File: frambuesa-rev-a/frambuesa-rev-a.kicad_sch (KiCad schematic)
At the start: 0 parts

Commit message: agregar chip y conexiones
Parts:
- added C1, C9: 1u, symbol Device:C
- added C10, C11, C2, C3, C4, C5, C6, C7, C8: 100n, symbol Device:C
- added R1, R2: R, symbol Device:R
- added U1: RP2040, Package_DFN_QFN:QFN-56-1EP_7x7mm_P0.4mm_EP3.2x3.2mm, symbol MCU_RaspberryPi:RP2040
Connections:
- new net: R2.2, U1.47 (USB_DP)
- new net: R1.2, U1.46 (USB_DM)
- new net +1V1: C10.1, C11.1, C9.1, U1.23 (DVDD), U1.45 (VREG_VOUT), U1.50 (DVDD)
- new net +3V3: C1.1, C2.1, C3.1, C4.1, C5.1, C6.1, C7.1, C8.1, U1.1 (IOVDD), U1.10 (IOVDD), U1.22 (IOVDD), U1.33 (IOVDD), U1.42 (IOVDD), U1.43 (ADC_AVDD), U1.44 (VREG_VIN), U1.48 (USB_VDD), U1.49 (IOVDD)
- new net GND: C1.2, C10.2, C11.2, C2.2, C3.2, C4.2, C5.2, C6.2, C7.2, C8.2, C9.2, U1.19 (TESTEN), U1.57 (GND)
- new net GPIO00: U1.2 (GPIO0)
- new net GPIO01: U1.3 (GPIO1)
- new net GPIO02: U1.4 (GPIO2)
- new net GPIO03: U1.5 (GPIO3)
- new net GPIO04: U1.6 (GPIO4)
- new net GPIO05: U1.7 (GPIO5)
- new net GPIO06: U1.8 (GPIO6)
- new net GPIO07: U1.9 (GPIO7)
- new net GPIO08: U1.11 (GPIO8)
- new net GPIO09: U1.12 (GPIO9)
- new net GPIO10: U1.13 (GPIO10)
- new net GPIO11: U1.14 (GPIO11)
- new net GPIO12: U1.15 (GPIO12)
- new net GPIO13: U1.16 (GPIO13)
- new net GPIO14: U1.17 (GPIO14)
- new net GPIO15: U1.18 (GPIO15)
- new net GPIO16: U1.27 (GPIO16)
- new net GPIO17: U1.28 (GPIO17)
- new net GPIO18: U1.29 (GPIO18)
- new net GPIO19: U1.30 (GPIO19)
- new net GPIO20: U1.31 (GPIO20)
- new net GPIO21: U1.32 (GPIO21)
- new net GPIO22: U1.34 (GPIO22)
- new net GPIO23: U1.35 (GPIO23)
- new net GPIO24: U1.36 (GPIO24)
- new net GPIO25: U1.37 (GPIO25)
- new net GPIO26_ADC0: U1.38 (GPIO26/ADC0)
- new net GPIO27_ADC1: U1.39 (GPIO27/ADC1)
- new net GPIO28_ADC2: U1.40 (GPIO28/ADC2)
- new net GPIO29_ADC3: U1.41 (GPIO29/ADC3)
- new net NOT_QSPI_SS: U1.56 (~{QSPI_SS})
- new net QSPI_SCLK: U1.52 (QSPI_SCLK)
- new net QSPI_SD0: U1.53 (QSPI_SD0)
- new net QSPI_SD1: U1.55 (QSPI_SD1)
- new net QSPI_SD2: U1.54 (QSPI_SD2)
- new net QSPI_SD3: U1.51 (QSPI_SD3)
- new net RUN: U1.26 (RUN)
- new net SWCLK: U1.24 (SWCLK)
- new net SWD: U1.25 (SWDIO)
- new net USB_D_MINUS: R1.1
- new net USB_D_PLUS: R2.1
- new net XIN: U1.20 (XIN)
- new net XOUT: U1.21 (XOUT)
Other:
- note added: "01: 02: a net label GPIO00 03: a net label GPIO01 04: a net label GPIO02 05: a net label GPIO03 06: a net label GPIO04 07: a net label GPIO05 08: a net label GPIO06 09: a net label GPIO07 10: 11: a net label GPIO08 12: a net label GPIO09 13: a net label GPIO10 14: a net label GPIO11 15: a net label GPIO12 16: a net label GPIO13 17: a net label GPIO14 18: a net label GPIO15 19: a GND 20: a net lab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"
- note added: "poder"
- company: (none) -> piruetas SpA

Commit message: agregar seccion poder
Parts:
- added C12, C13: 10u, symbol Device:C
- added J1: USB_B_Micro, symbol Connector:USB_B_Micro
- added U2: NCP1117-3.3_SOT223, Package_TO_SOT_SMD:SOT-223-3_TabPin2, symbol Regulator_Linear:NCP1117-3.3_SOT223
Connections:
- net +3V3: now also C13.1, U2.2 (VO)
- net GND: now also C12.2, C13.2, J1.5 (GND), J1.SH (Shield), U2.1 (GND)
- net USB_D_MINUS: now also J1.2 (D-)
- net USB_D_PLUS: now also J1.3 (D+)
- new net VBUS: C12.1, J1.1 (VBUS), U2.3 (VI)
- no-connect marks 0 -> 1

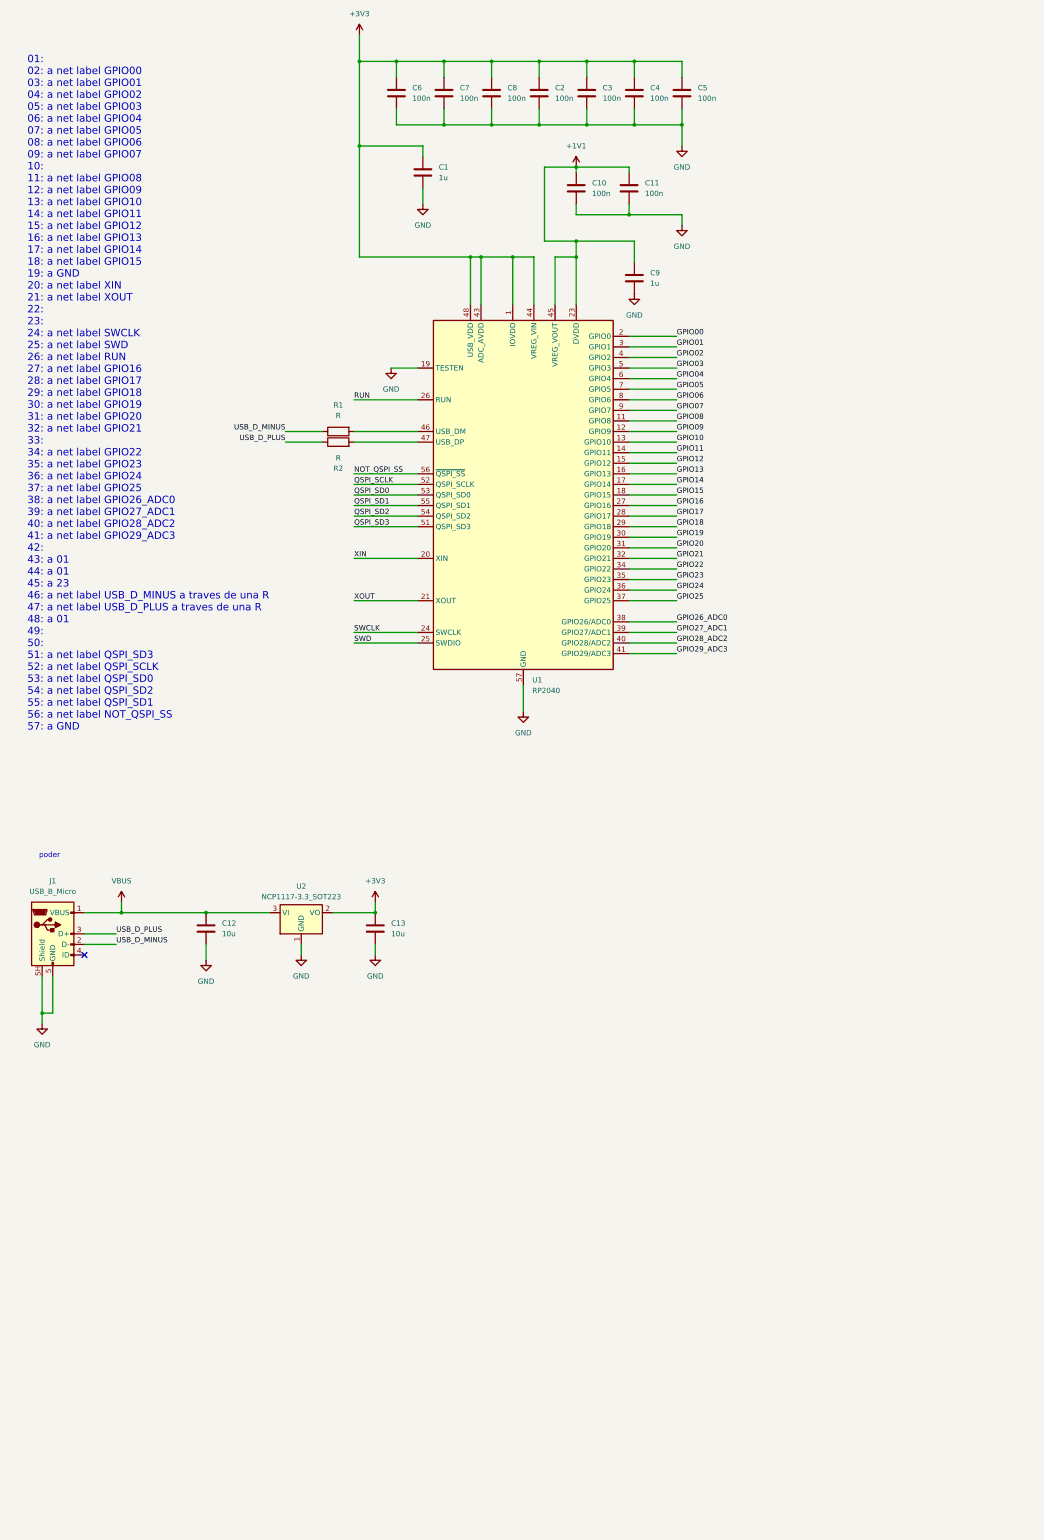
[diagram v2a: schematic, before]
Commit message: agregar cristal, mounting holes
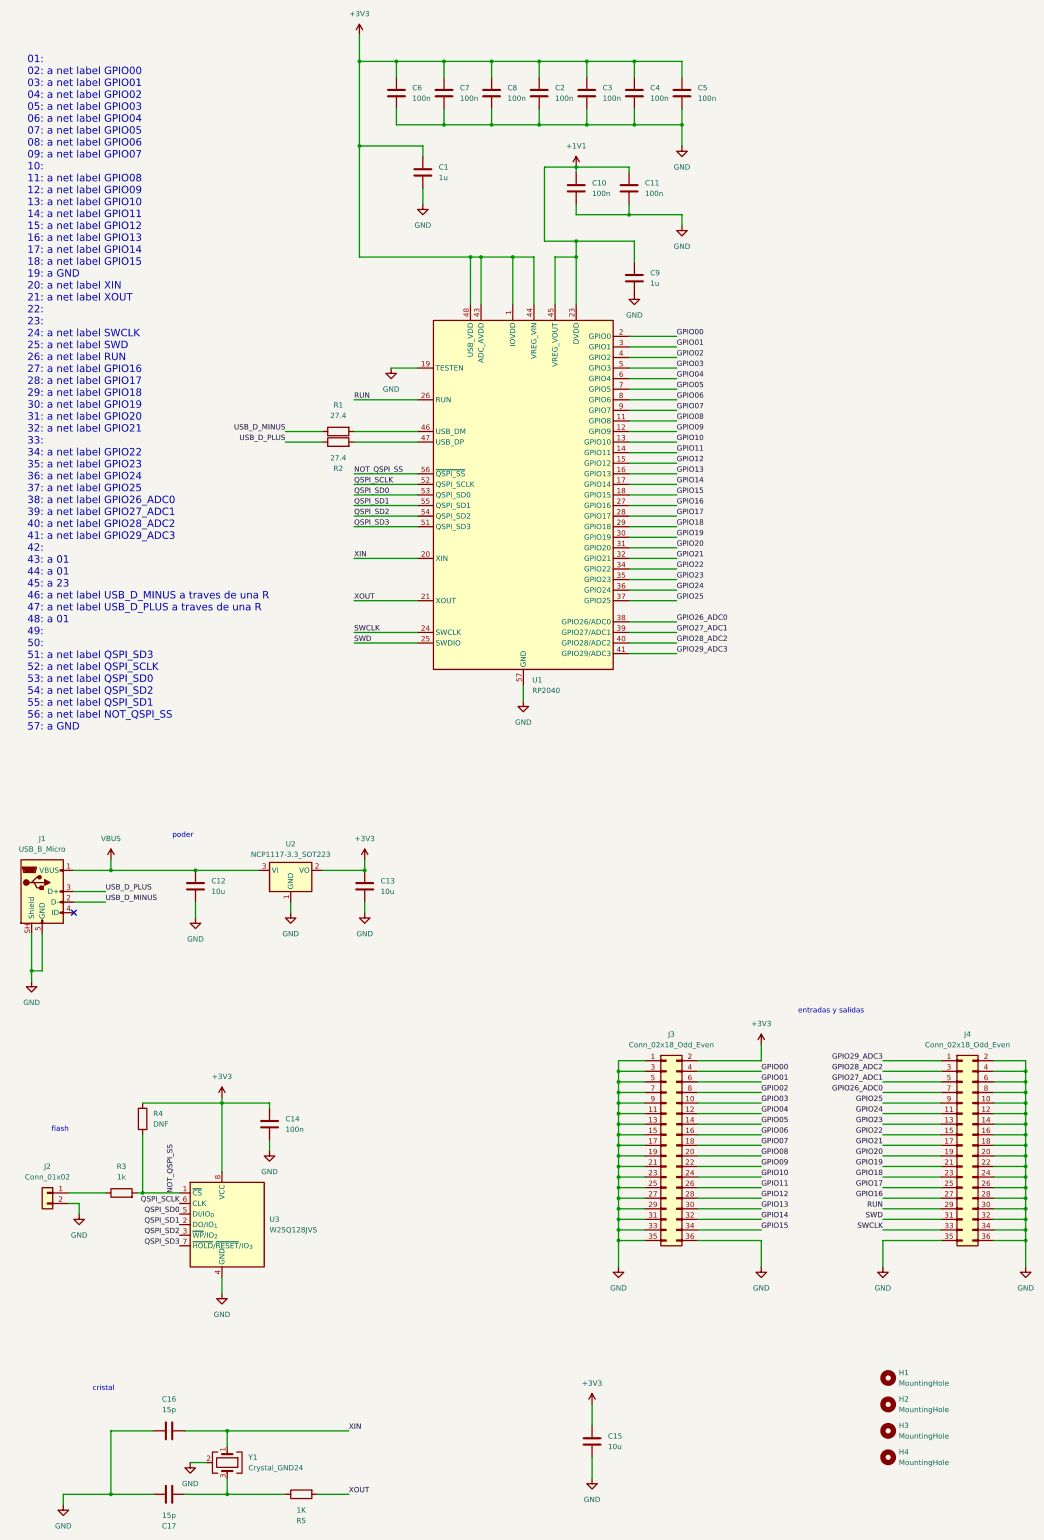
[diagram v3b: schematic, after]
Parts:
- added C14: 100n, symbol Device:C
- added C15: 10u, symbol Device:C
- added C16, C17: 15p, symbol Device:C
- added H1, H2, H3, H4: MountingHole, symbol Mechanical:MountingHole
- added J2: Conn_01x02, symbol Connector_Generic:Conn_01x02
- added J3, J4: Conn_02x18_Odd_Even, symbol Connector_Generic:Conn_02x18_Odd_Even
- added R3: 1k, symbol Device:R
- added R4: DNF, symbol Device:R
- added R5: 1K, symbol Device:R
- added U3: W25Q128JVS, Package_SO:SOIC-8_5.3x5.3mm_P1.27mm, symbol Memory_Flash:W25Q128JVS
- added Y1: Crystal_GND24, symbol Device:Crystal_GND24
- R1, R2: value R -> 27.4
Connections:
- net +3V3: now also C14.1, C15.1, J3.2 (Pin_2), R4.1, U3.8 (VCC)
- net GND: now also C14.2, C15.2, C16.1, C17.1, J2.2 (Pin_2), J3.1 (Pin_1), J3.11 (Pin_11), J3.13 (Pin_13), J3.15 (Pin_15), J3.17 (Pin_17), J3.19 (Pin_19), J3.21 (Pin_21), J3.23 (Pin_23), J3.25 (Pin_25), J3.27 (Pin_27), J3.29 (Pin_29), J3.3 (Pin_3), J3.31 (Pin_31), J3.33 (Pin_33), J3.35 (Pin_35), J3.36 (Pin_36), J3.5 (Pin_5), J3.7 (Pin_7), J3.9 (Pin_9), J4.10 (Pin_10), J4.12 (Pin_12), J4.14 (Pin_14), J4.16 (Pin_16), J4.18 (Pin_18), J4.2 (Pin_2), J4.20 (Pin_20), J4.22 (Pin_22), J4.24 (Pin_24), J4.26 (Pin_26), J4.28 (Pin_28), J4.30 (Pin_30), J4.32 (Pin_32), J4.34 (Pin_34), J4.35 (Pin_35), J4.36 (Pin_36), J4.4 (Pin_4), J4.6 (Pin_6), J4.8 (Pin_8), U3.4 (GND), Y1.2 (G), Y1.4 (G)
- net GPIO00: now also J3.4 (Pin_4)
- net GPIO01: now also J3.6 (Pin_6)
- net GPIO02: now also J3.8 (Pin_8)
- net GPIO03: now also J3.10 (Pin_10)
- net GPIO04: now also J3.12 (Pin_12)
- net GPIO05: now also J3.14 (Pin_14)
- net GPIO06: now also J3.16 (Pin_16)
- net GPIO07: now also J3.18 (Pin_18)
- net GPIO08: now also J3.20 (Pin_20)
- net GPIO09: now also J3.22 (Pin_22)
- net GPIO10: now also J3.24 (Pin_24)
- net GPIO11: now also J3.26 (Pin_26)
- net GPIO12: now also J3.28 (Pin_28)
- net GPIO13: now also J3.30 (Pin_30)
- net GPIO14: now also J3.32 (Pin_32)
- net GPIO15: now also J3.34 (Pin_34)
- net GPIO16: now also J4.27 (Pin_27)
- net GPIO17: now also J4.25 (Pin_25)
- net GPIO18: now also J4.23 (Pin_23)
- net GPIO19: now also J4.21 (Pin_21)
- net GPIO20: now also J4.19 (Pin_19)
- net GPIO21: now also J4.17 (Pin_17)
- net GPIO22: now also J4.15 (Pin_15)
- net GPIO23: now also J4.13 (Pin_13)
- net GPIO24: now also J4.11 (Pin_11)
- net GPIO25: now also J4.9 (Pin_9)
- net GPIO26_ADC0: now also J4.7 (Pin_7)
- net GPIO27_ADC1: now also J4.5 (Pin_5)
- net GPIO28_ADC2: now also J4.3 (Pin_3)
- net GPIO29_ADC3: now also J4.1 (Pin_1)
- net NOT_QSPI_SS: now also R3.2, R4.2, U3.1 (~{CS})
- net QSPI_SCLK: now also U3.6 (CLK)
- net QSPI_SD0: now also U3.5 (DI/IO_{0})
- net QSPI_SD1: now also U3.2 (DO/IO_{1})
- net QSPI_SD2: now also U3.3 (~{WP}/IO_{2})
- net QSPI_SD3: now also U3.7 (~{HOLD}/~{RESET}/IO_{3})
- net RUN: now also J4.29 (Pin_29)
- net SWCLK: now also J4.33 (Pin_33)
- net SWD: now also J4.31 (Pin_31)
- net XIN: now also C16.2, Y1.1
- net XOUT: now also R5.2
- new net: J2.1 (Pin_1), R3.1
- new net: C17.2, R5.1, Y1.3
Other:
- note added: "cristal"
- note added: "entradas y salidas"
- note added: "flash"
- moved on the sheet: C12, C13, J1, U2

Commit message: agregar footprints m3
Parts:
- H1, H2, H3, H4: footprint (none) -> MountingHole:MountingHole_3.2mm_M3
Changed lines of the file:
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@@
 			)
 		)
-		(property "Footprint" ""
+		(property "Footprint" "MountingHole:MountingHole_3.2mm_M3"
 			(at 229.87 367.03 0)
 			(hide yes)
@@
 			)
 		)
-		(property "Footprint" ""
+		(property "Footprint" "MountingHole:MountingHole_3.2mm_M3"
 			(at 229.87 360.68 0)
 			(hide yes)
@@
 			)
 		)
-		(property "Footprint" ""
+		(property "Footprint" "MountingHole:MountingHole_3.2mm_M3"
 			(at 229.87 347.98 0)
 			(hide yes)
@@
 			)
 		)
-		(property "Footprint" ""
+		(property "Footprint" "MountingHole:MountingHole_3.2mm_M3"
 			(at 229.87 354.33 0)
 			(hide yes)

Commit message: agregar mas footprints
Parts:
- C1, C10, C11, C14, C2, C3, C4, C5, C6, C7, C8, C9: footprint (none) -> Capacitor_SMD:C_0805_2012Metric
- C12, C13, C15: footprint (none) -> Capacitor_SMD:CP_Elec_4x5.4
- R3, R5: footprint (none) -> Resistor_SMD:R_0805_2012Metric
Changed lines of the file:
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@@
 			)
 		)
-		(property "Footprint" ""
+		(property "Footprint" "Capacitor_SMD:C_0805_2012Metric"
 			(at 168.6052 66.04 0)
 			(hide yes)
@@
 			)
 		)
-		(property "Footprint" ""
+		(property "Footprint" "Resistor_SMD:R_0805_2012Metric"
 			(at 45.72 305.308 90)
 			(hide yes)
@@
 			)
 		)
-		(property "Footprint" ""
+		(property "Footprint" "Capacitor_SMD:C_0805_2012Metric"
 			(at 155.9052 66.04 0)
 			(hide yes)
@@
 			)
 		)
-		(property "Footprint" ""
+		(property "Footprint" "Capacitor_SMD:C_0805_2012Metric"
 			(at 147.0152 43.18 0)
 			(hide yes)
@@
 			)
 		)
-		(property "Footprint" ""
+		(property "Footprint" "Capacitor_SMD:C_0805_2012Metric"
 			(at 169.8752 87.63 0)
 			(hide yes)
@@
 			)
 		)
-		(property "Footprint" ""
+		(property "Footprint" "Capacitor_SMD:C_0805_2012Metric"
 			(at 158.4452 43.18 0)
 			(hide yes)
@@
 			)
 		)
-		(property "Footprint" ""
+		(property "Footprint" "Capacitor_SMD:CP_Elec_4x5.4"
 			(at 64.4652 233.68 0)
 			(hide yes)
@@
 			)
 		)
-		(property "Footprint" ""
+		(property "Footprint" "Resistor_SMD:R_0805_2012Metric"
 			(at 88.9 374.142 90)
 			(hide yes)
@@
 			)
 		)
-		(property "Footprint" ""
+		(property "Footprint" "Capacitor_SMD:C_0805_2012Metric"
 			(at 135.5852 43.18 0)
 			(hide yes)
@@
 			)
 		)
-		(property "Footprint" ""
+		(property "Footprint" "Capacitor_SMD:C_0805_2012Metric"
 			(at 181.3052 43.18 0)
 			(hide yes)
@@
 			)
 		)
-		(property "Footprint" ""
+		(property "Footprint" "Capacitor_SMD:C_0805_2012Metric"
 			(at 119.0752 62.23 0)
 			(hide yes)
@@
 			)
 		)
-		(property "Footprint" ""
+		(property "Footprint" "Capacitor_SMD:CP_Elec_4x5.4"
 			(at 105.1052 233.68 0)
 			(hide yes)
@@
 			)
 		)
-		(property "Footprint" ""
+		(property "Footprint" "Capacitor_SMD:C_0805_2012Metric"
 			(at 169.8752 43.18 0)
 			(hide yes)
@@
 			)
 		)
-		(property "Footprint" ""
+		(property "Footprint" "Capacitor_SMD:C_0805_2012Metric"
 			(at 112.7252 43.18 0)
 			(hide yes)
@@
 			)
 		)
-		(property "Footprint" ""
+		(property "Footprint" "Capacitor_SMD:CP_Elec_4x5.4"
 			(at 159.7152 367.03 0)
 			(hide yes)
@@
 			)
 		)
-		(property "Footprint" ""
+		(property "Footprint" "Capacitor_SMD:C_0805_2012Metric"
 			(at 124.1552 43.18 0)
 			(hide yes)
@@
 			)
 		)
-		(property "Footprint" ""
+		(property "Footprint" "Capacitor_SMD:C_0805_2012Metric"
 			(at 82.2452 290.83 0)
 			(hide yes)

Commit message: cambiar tamano, borrar tracks
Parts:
- J3, J4: footprint (none) -> Connector_PinSocket_2.54mm:PinSocket_1x20_P2.54mm_Vertical
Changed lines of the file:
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@@
 			)
 		)
-		(property "Footprint" ""
+		(property "Footprint" "Connector_PinSocket_2.54mm:PinSocket_1x20_P2.54mm_Vertical"
 			(at 176.53 292.1 0)
 			(hide yes)
@@
 			)
 		)
-		(property "Footprint" ""
+		(property "Footprint" "Connector_PinSocket_2.54mm:PinSocket_1x20_P2.54mm_Vertical"
 			(at 247.65 292.1 0)
 			(hide yes)
